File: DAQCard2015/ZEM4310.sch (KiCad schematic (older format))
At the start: 2 parts, among them P1 QTH-090-01-F-D-A, P2 QTH-090-01-F-D-A

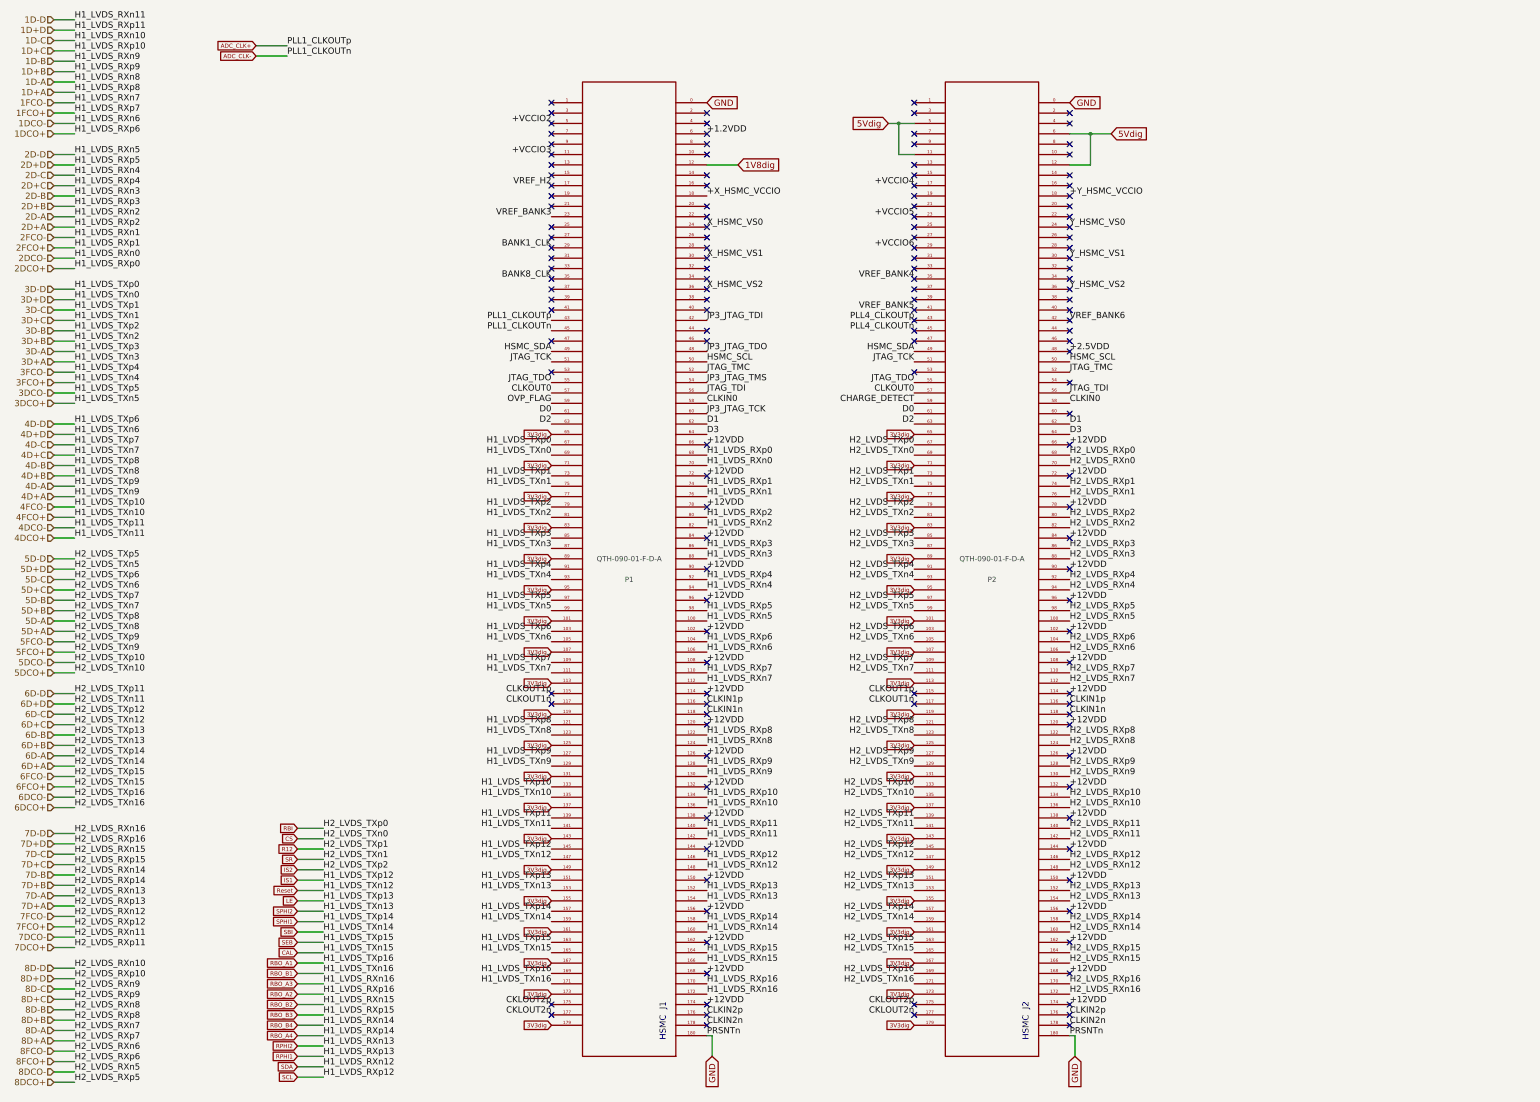
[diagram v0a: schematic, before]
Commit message: Adds misc traces(gnds, SPI, etc) to DAQ board
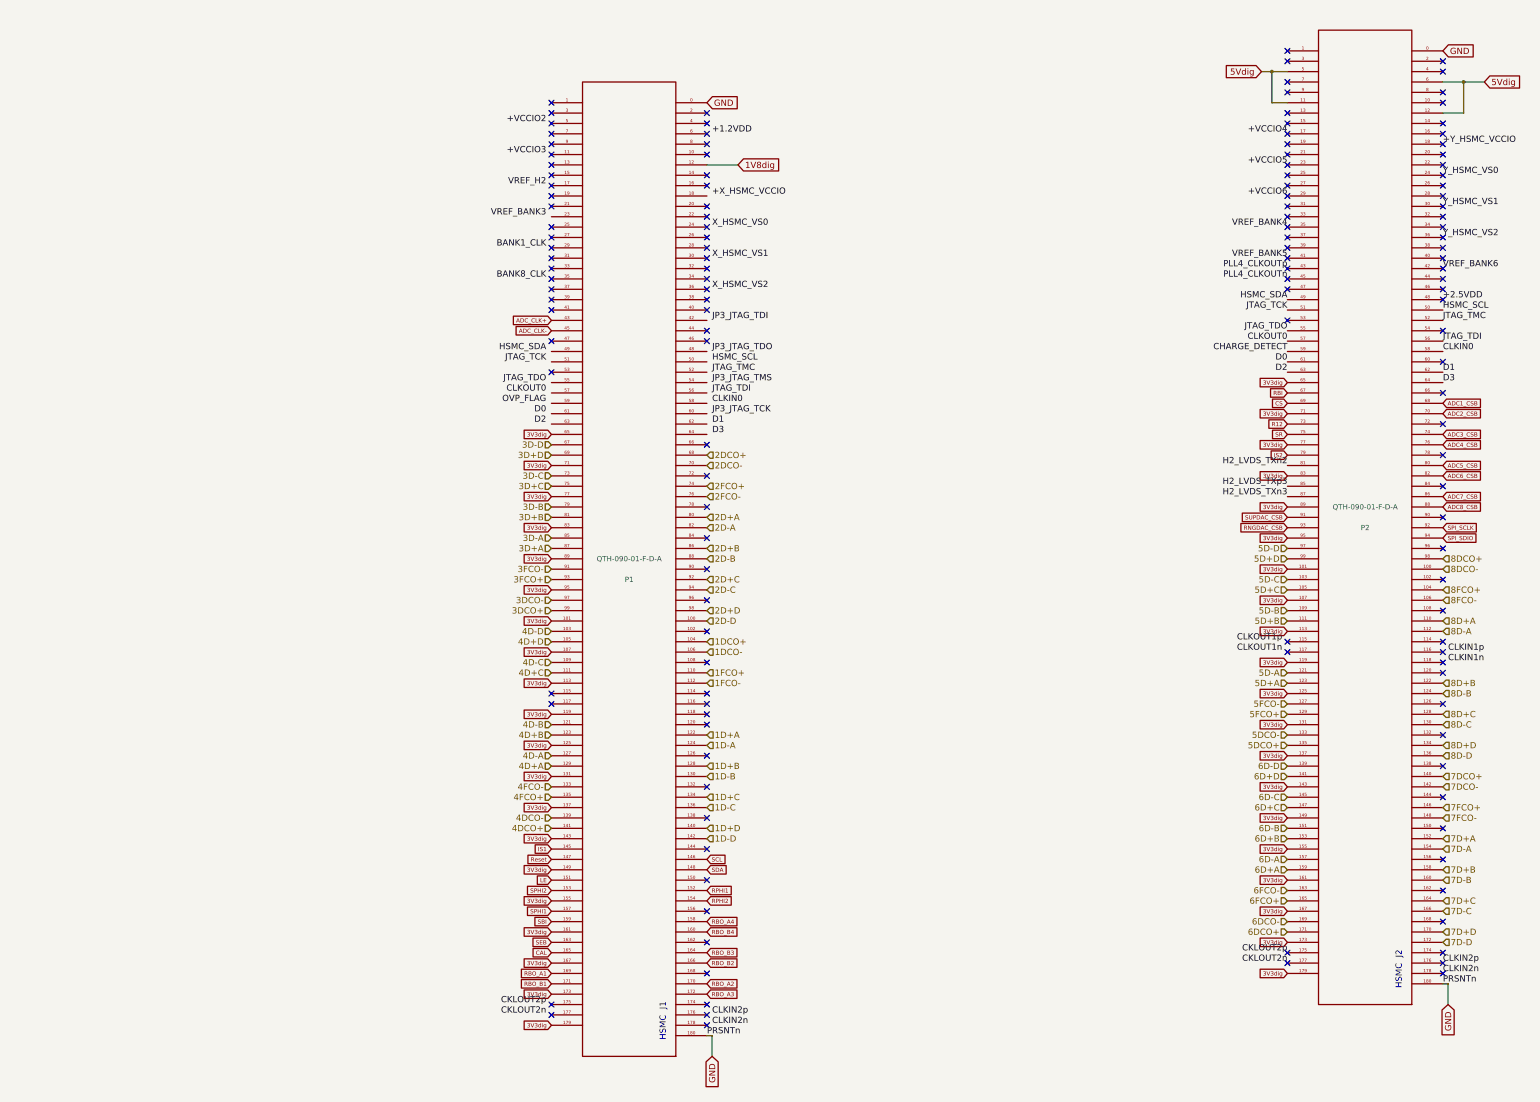
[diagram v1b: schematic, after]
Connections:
- net +1.2VDD: no longer P1.6
- net +VCCIO2: no longer P1.5
- net +VCCIO3: no longer P1.11
- net +X_HSMC_VCCIO: no longer P1.18
- net BANK1_CLK: no longer P1.29
- net BANK8_CLK: no longer P1.35
- net CKLOUT2n: no longer P1.177
- net CKLOUT2p: no longer P1.175
- net CLKIN0: no longer P1.58
- net CLKIN1n: no longer P1.118, P2.118
- net CLKIN1p: no longer P1.116, P2.116
- net CLKIN2n: no longer P1.178
- net CLKIN2p: no longer P1.176
- net CLKOUT0: no longer P1.57
- net CLKOUT1n: no longer P1.117, P2.117
- net CLKOUT1p: no longer P1.115, P2.115
- net D0: no longer P1.61
- net D1: no longer P1.62
- net D2: no longer P1.63
- net D3: no longer P1.64
- net HSMC_SCL: no longer P1.50
- net HSMC_SDA: no longer P1.49
- net JP3_JTAG_TCK: no longer P1.60
- net JP3_JTAG_TDI: no longer P1.42
- net JP3_JTAG_TDO: no longer P1.48
- net JP3_JTAG_TMS: no longer P1.54
- net JTAG_TCK: no longer P1.51
- net JTAG_TDI: no longer P1.56
- net JTAG_TDO: no longer P1.55
- net JTAG_TMC: no longer P1.52
- net OVP_FLAG: no longer P1.59
- net VREF_BANK3: no longer P1.23
- net VREF_H2: no longer P1.17
- net X_HSMC_VS0: no longer P1.24
- net X_HSMC_VS1: no longer P1.30
- net X_HSMC_VS2: no longer P1.36
- removed net +12VDD: P1.102, P1.108, P1.114, P1.120, P1.126, P1.132, P1.138, P1.144, P1.150, P1.156, P1.162, P1.168, P1.174, P1.66, P1.72, P1.78, P1.84, P1.90, P1.96, P2.102, P2.108, P2.114, P2.120, P2.126, P2.132, P2.138, P2.144, P2.150, P2.156, P2.162, P2.168, P2.174, P2.66, P2.72, P2.78, P2.84, P2.90, P2.96
- net H2_LVDS_RXn0 renamed ADC2_CSB
- net H2_LVDS_RXn1 renamed ADC4_CSB
- net H2_LVDS_RXn2 renamed ADC6_CSB
- net H2_LVDS_RXn3 renamed ADC8_CSB
- net H2_LVDS_RXn4 renamed SPI_SDIO
- net H2_LVDS_RXp0 renamed ADC1_CSB
- net H2_LVDS_RXp1 renamed ADC3_CSB
- net H2_LVDS_RXp2 renamed ADC5_CSB
- net H2_LVDS_RXp3 renamed ADC7_CSB
- net H2_LVDS_RXp4 renamed SPI_SCLK
- net H2_LVDS_TXn4 renamed RNGDAC_CSB
- net H2_LVDS_TXp4 renamed SUPDAC_CSB
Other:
- moved on the sheet: P2

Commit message: Update to DAQ Board including adding an JTAG header and hooking up external clock and trigger
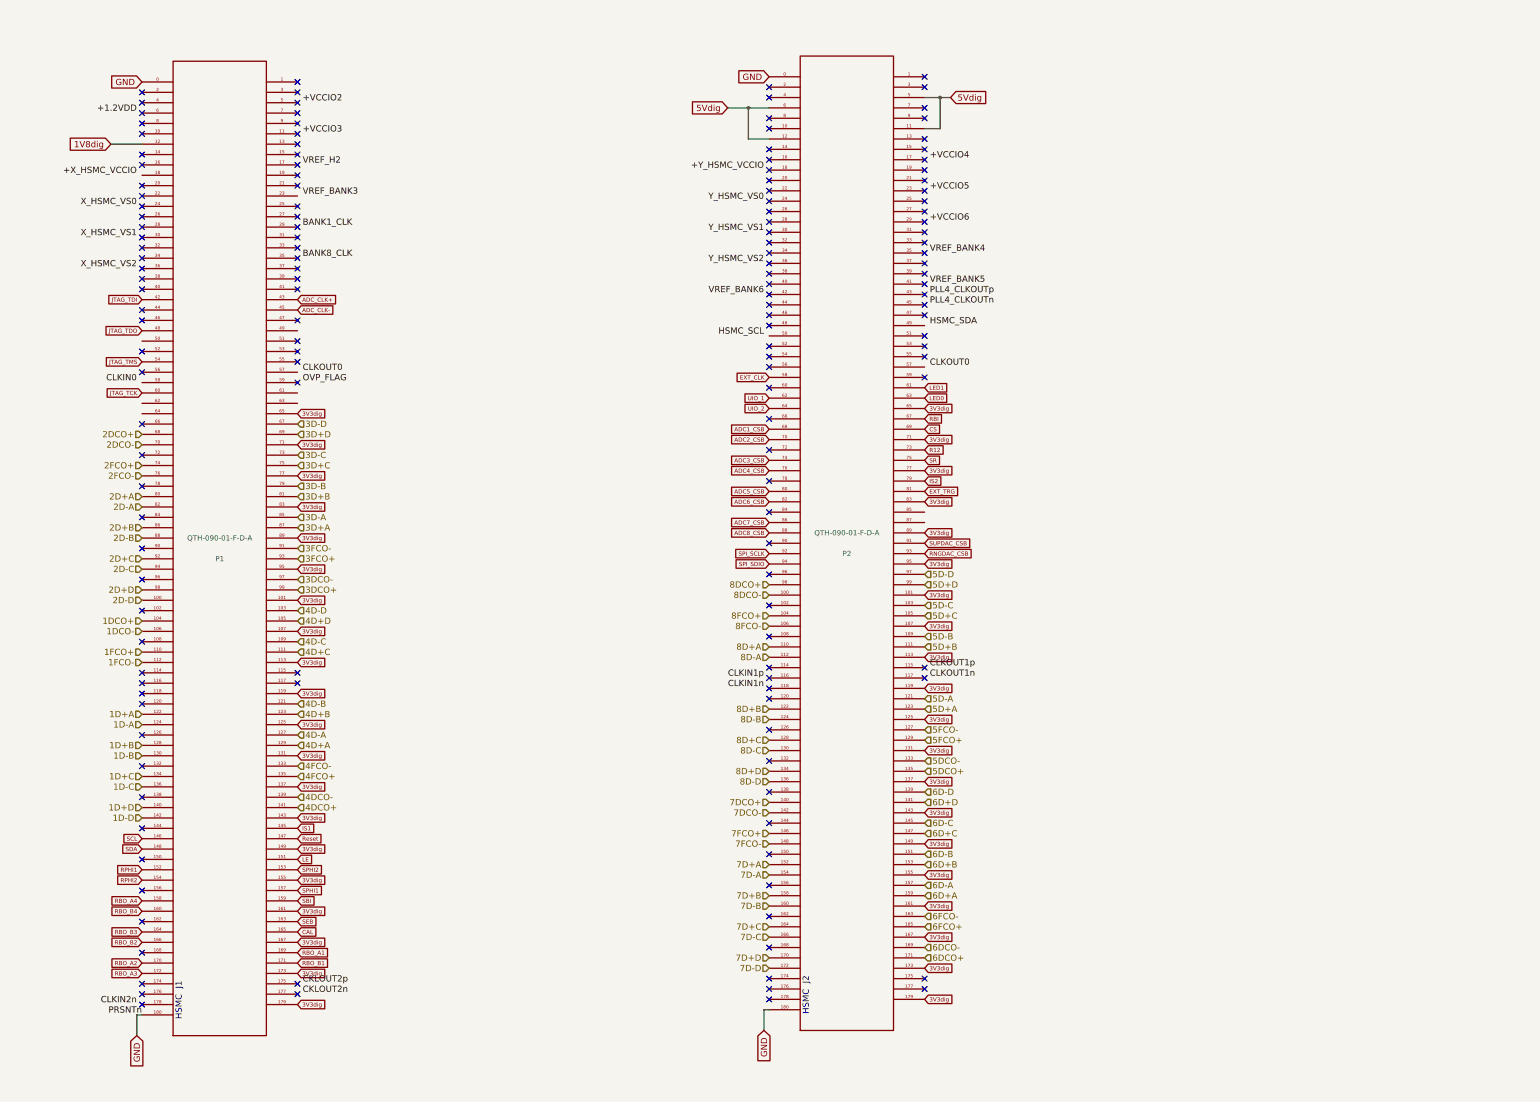
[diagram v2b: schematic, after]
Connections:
- net +VCCIO4: no longer P2.17
- net +VCCIO5: no longer P2.23
- net +VCCIO6: no longer P2.29
- net +Y_HSMC_VCCIO: no longer P2.18
- net CKLOUT2n: no longer P2.177
- net CKLOUT2p: no longer P2.175
- net CLKIN0: no longer P2.58
- net CLKIN2n: no longer P2.178
- net CLKOUT0: no longer P2.57
- net HSMC_SCL: no longer P2.50
- net HSMC_SDA: no longer P2.49
- net JTAG_TCK: now also P1.60; no longer P2.51
- net JTAG_TDI: now also P1.42; no longer P2.56
- net JTAG_TDO: now also P1.48; no longer P2.55
- net PLL4_CLKOUTn: no longer P2.45
- net PLL4_CLKOUTp: no longer P2.43
- net VREF_BANK4: no longer P2.35
- net VREF_BANK5: no longer P2.41
- net VREF_BANK6: no longer P2.42
- net Y_HSMC_VS0: no longer P2.24
- net Y_HSMC_VS1: no longer P2.30
- net Y_HSMC_VS2: no longer P2.36
- net JTAG_TMS: now reaches P1.54
- net +2.5VDD: no longer names the net of P2.48
- net CHARGE_DETECT: no longer names the net of P2.59
- net CLKIN2p: no longer names the net of P2.176
- net D0 renamed LED1
- net D1 renamed UIO_1
- net D2 renamed LED0
- net D3 renamed UIO_2
- net H2_LVDS_TXn2 renamed EXT_TRG
- net H2_LVDS_TXn3: no longer names the net of P2.87
- net H2_LVDS_TXp3: no longer names the net of P2.85
- net JTAG_TMC: no longer names the net of P2.52
- new net EXT_CLK: P2.58
- no-connect marks 143 -> 153
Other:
- moved on the sheet: P1, P2

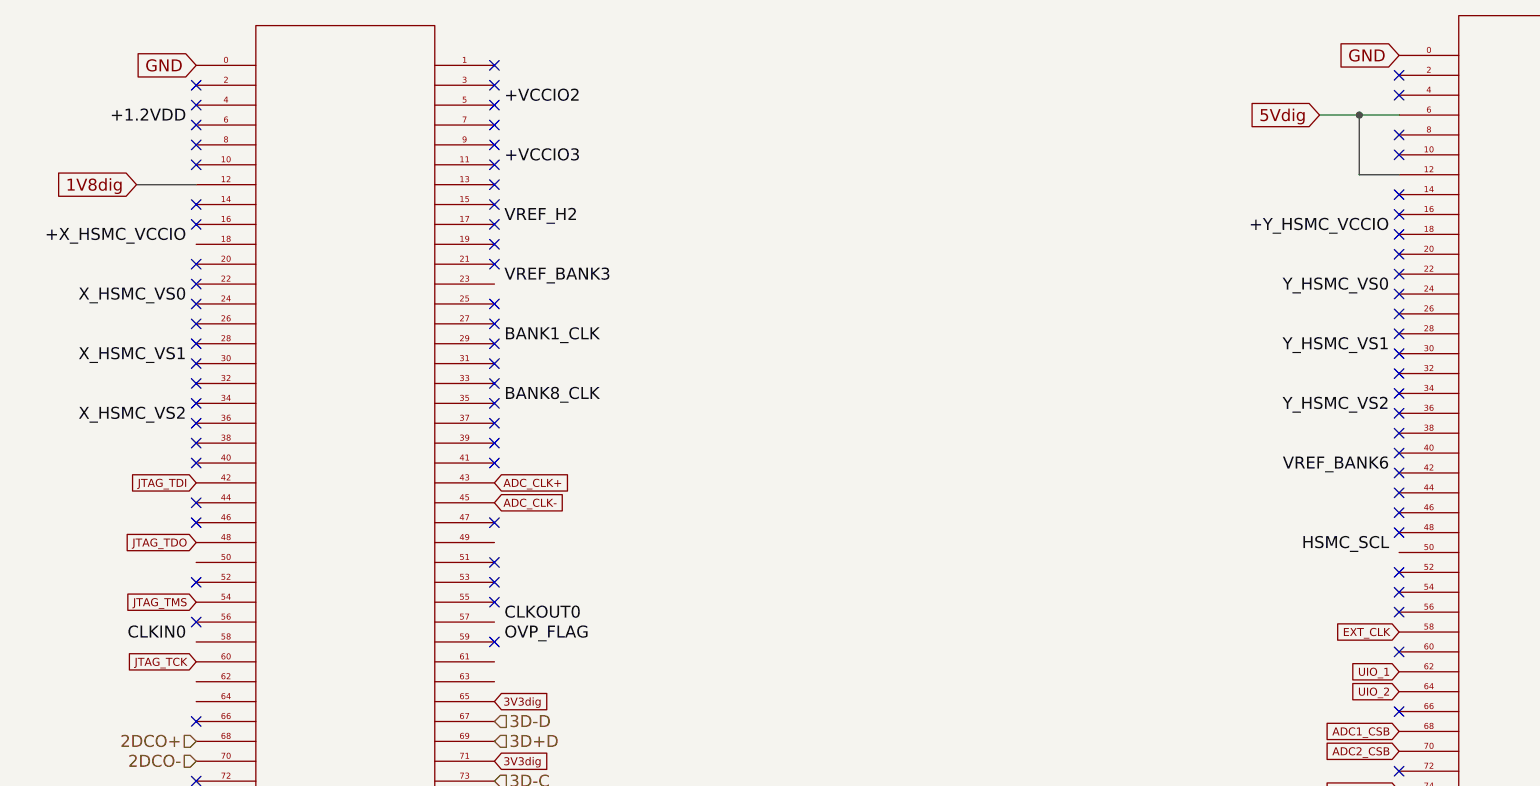
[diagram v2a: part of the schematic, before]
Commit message: Moves external clock to dedicated clock input
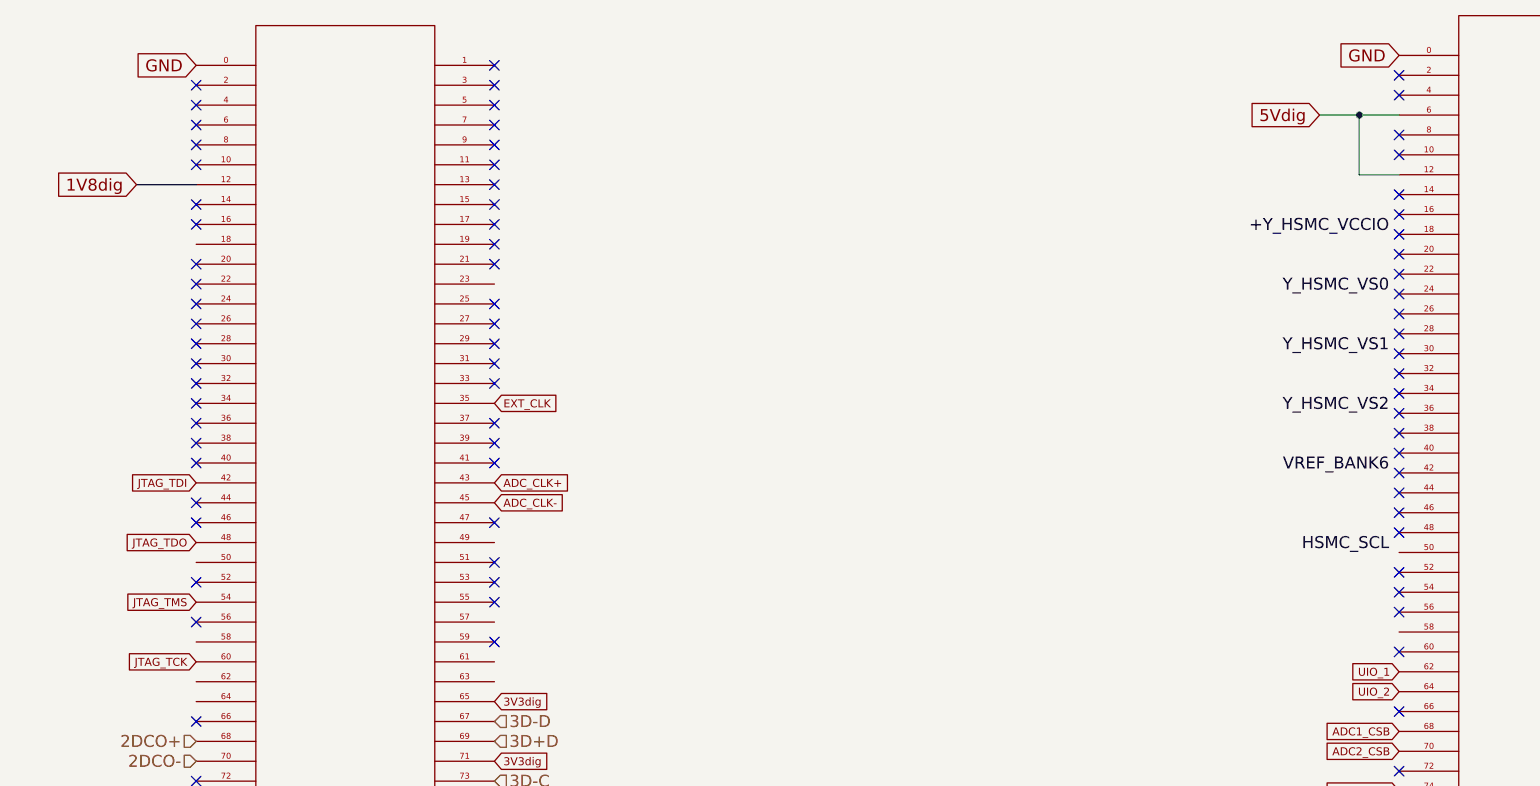
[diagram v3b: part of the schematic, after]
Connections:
- net EXT_CLK: now also P1.35; no longer P2.58
- no-connect marks 153 -> 152
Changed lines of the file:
@@
 NoConn ~ 3450 1450
 NoConn ~ 1950 1550
-Text Label 3500 1550 0    60   ~ 0
-+VCCIO2
-Text Label 1900 1650 2    60   ~ 0
-+1.2VDD
 NoConn ~ 3450 1650
 NoConn ~ 3450 1750
 NoConn ~ 1950 1750
 NoConn ~ 1950 1850
-Text Label 3500 1850 0    60   ~ 0
-+VCCIO3
 NoConn ~ 3450 1950
 NoConn ~ 3450 2050
 NoConn ~ 1950 2050
 NoConn ~ 1950 2150
-Text Label 3500 2150 0    60   ~ 0
-VREF_H2
-Text Label 1900 2250 2    60   ~ 0
-+X_HSMC_VCCIO
 NoConn ~ 1950 2450
 NoConn ~ 1950 2350
 NoConn ~ 3450 2350
 NoConn ~ 3450 2250
-Text Label 3500 2450 0    60   ~ 0
-VREF_BANK3
-Text Label 1900 2550 2    60   ~ 0
-X_HSMC_VS0
 NoConn ~ 3450 2550
 NoConn ~ 3450 2650
 NoConn ~ 1950 2650
 NoConn ~ 1950 2750
-Text Label 3500 2750 0    60   ~ 0
-BANK1_CLK
-Text Label 1900 2850 2    60   ~ 0
-X_HSMC_VS1
 NoConn ~ 1950 2950
 NoConn ~ 1950 3050
 NoConn ~ 3450 2850
 NoConn ~ 3450 2950
-Text Label 1900 3150 2    60   ~ 0
-X_HSMC_VS2
-Text Label 3500 3050 0    60   ~ 0
-BANK8_CLK
 NoConn ~ 1950 3250
 NoConn ~ 1950 3350
@@
 NoConn ~ 3450 3650
 NoConn ~ 3450 3950
-Text Label 3500 4150 0    60   ~ 0
-CLKOUT0
-Text Label 1900 4250 2    60   ~ 0
-CLKIN0
-Text Label 3500 4250 0    60   ~ 0
-OVP_FLAG
 Text Label 1950 10350 2    60   ~ 0
 PRSNTn
@@
 NoConn ~ 1950 2850
 NoConn ~ 1950 3150
-NoConn ~ 3450 3050
 NoConn ~ 3450 2750
 NoConn ~ 3450 2150
@@
 NoConn ~ 1950 4150
 NoConn ~ 3450 4250
-Text GLabel 8000 4200 0    40   Input ~ 0
+Text GLabel 3450 3050 2    40   Input ~ 0
 EXT_CLK
 NoConn ~ 8000 4100
